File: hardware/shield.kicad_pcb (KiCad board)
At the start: 4 copper layers, 117.7 x 100.9 mm, 47 parts, among them J1 Battery, J10 Right Photo Cell, J11 <-Front Center Distance, J13 Bump1, J14 Bump2, J15 Bump3, J16 PIR, J17 Front Right Distance, J18 Back Right Distance, J19 Left Cliff, J2 3.3V 500mA Regulator, J20 Right Cliff, J21 OLED, J22 LMotor-1, J23 RMotor-1, J24 LMotor-2, J25 RMotor-2, J26 Left Motor, J27 RightMotor Conn, J3 5.0V 500mA Regulator, J4 12V Boost Regulator, J5 Left Photo, J6 Front Left Distance, J7 Back Left Distance, J8 IMU-1, J9 IMU-2, P10 CONN_01X01, P11 CONN_01X01, P12 CONN_01X01, P2 Power, P3 Analog, P5 GPIO, P6 GPIO, P7 GPIO, P8 CONN_01X01, P9 CONN_01X01, U1 MCP23018

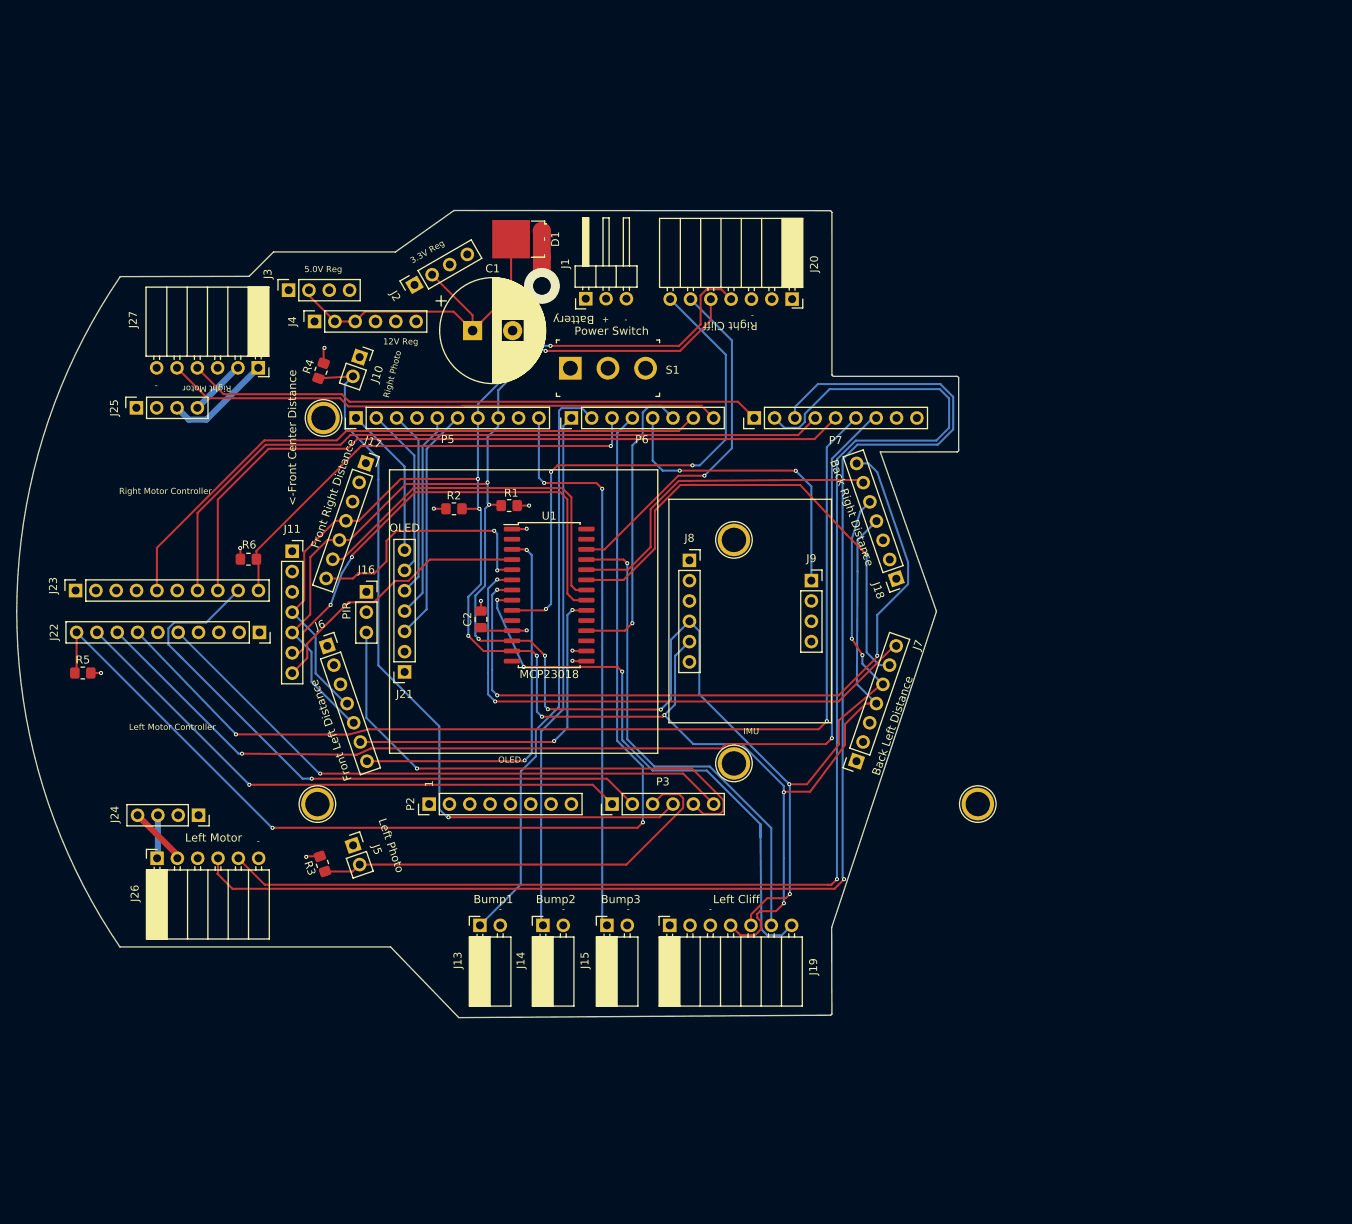
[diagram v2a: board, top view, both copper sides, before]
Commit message: Re-align schematic to PCB
While laying out the PCB, I modified the footprints used for the
headers connecting to the nRF52-DK and changed some of the header value
names. This commit makes the same updates to the schematic sheets.
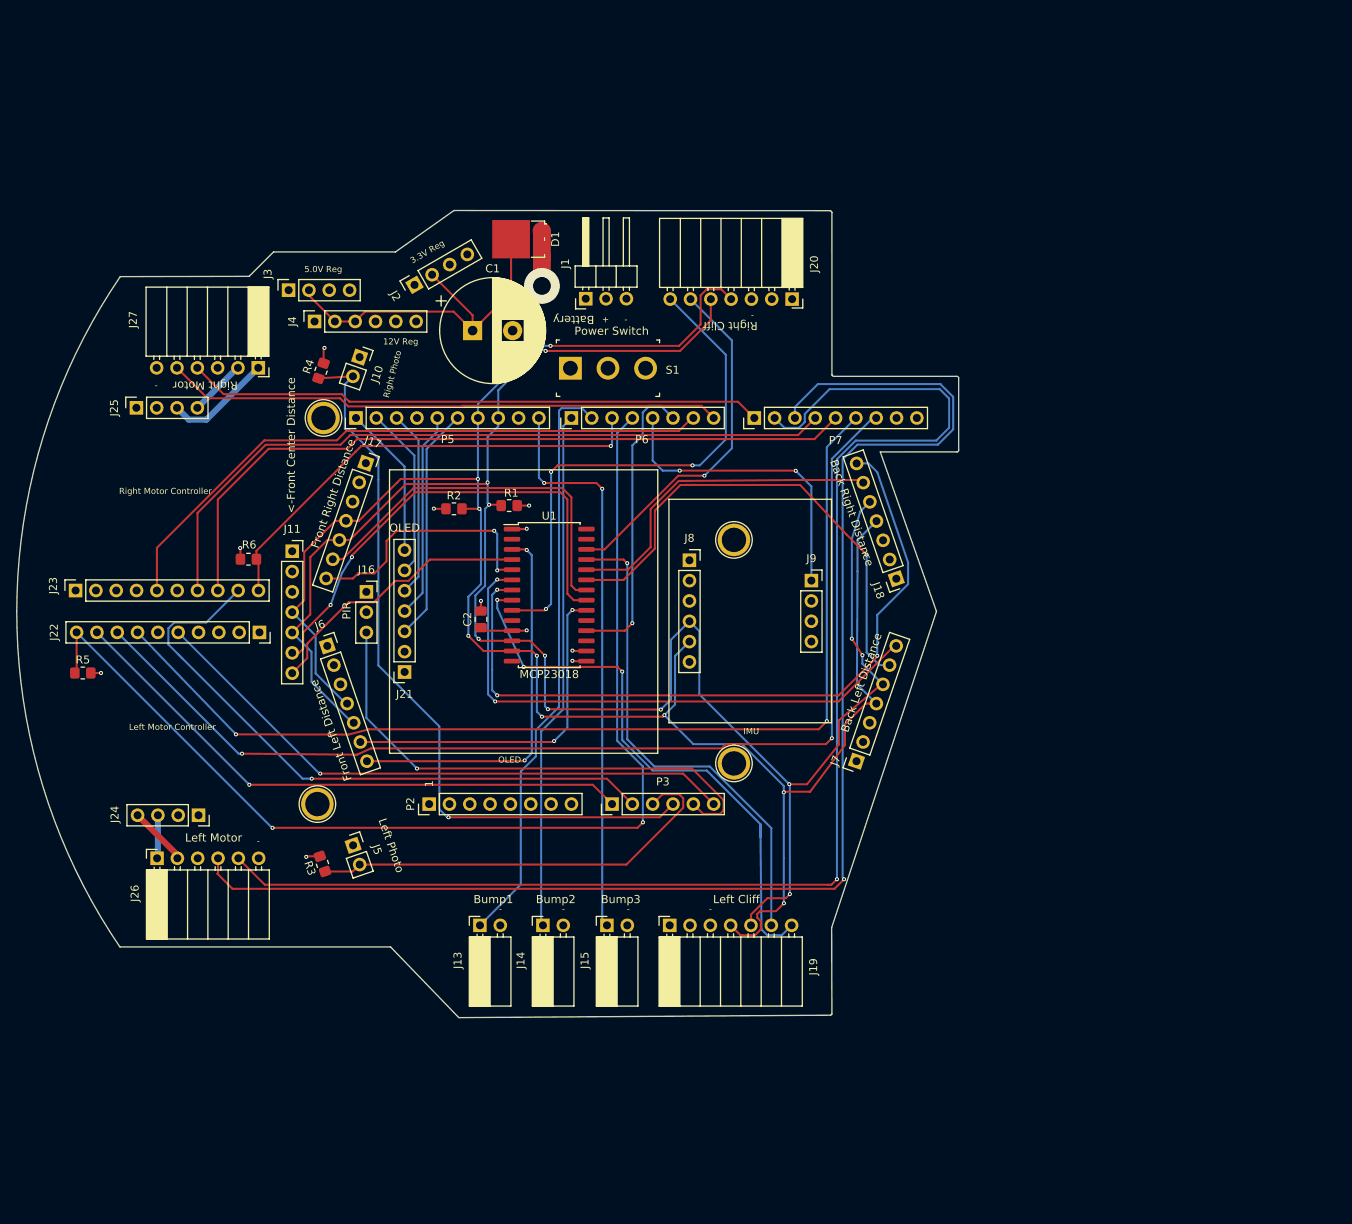
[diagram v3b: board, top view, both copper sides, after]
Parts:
- removed P10: CONN_01X01, Socket_Arduino_Mega:Arduino_1pin
- J11: value <-Front Center Distance -> Front Center Distance
- J27: value RightMotor Conn -> Right Motor
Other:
- board text added: "<-Front Center Distance"
- board text removed: "Right Motor"
